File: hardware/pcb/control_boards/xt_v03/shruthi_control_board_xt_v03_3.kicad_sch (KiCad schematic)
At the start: 50 parts, among them IC2 74HC165N, IC3 74HC165N, IC8 74595N, IC9 74HC165N, SW1 Encoder

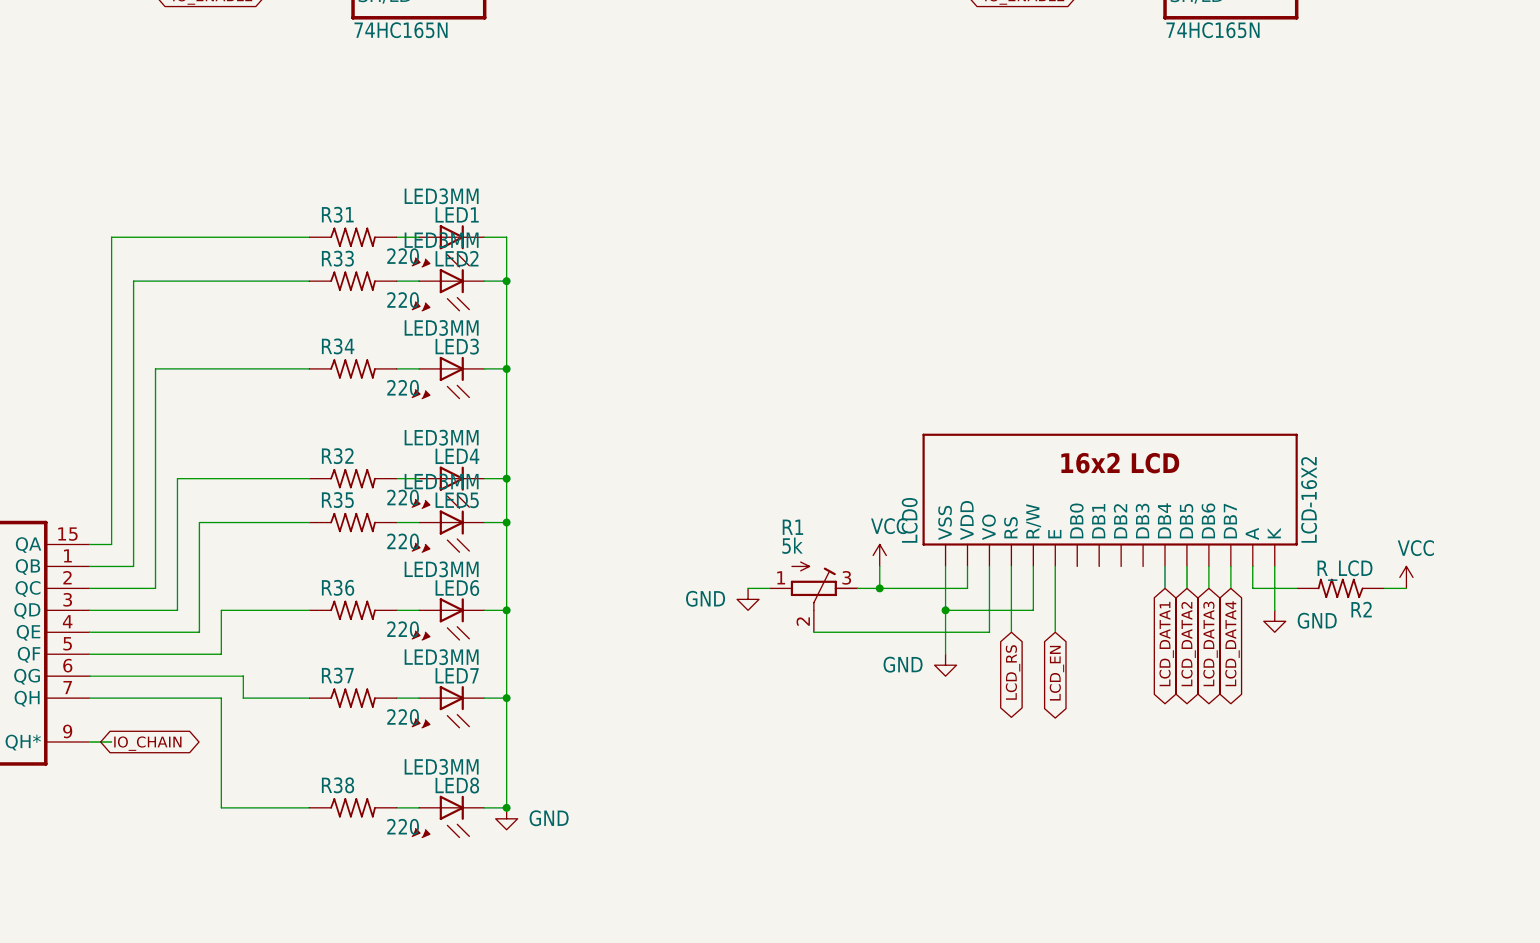
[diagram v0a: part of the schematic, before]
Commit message: update resistors to use kicad symbols
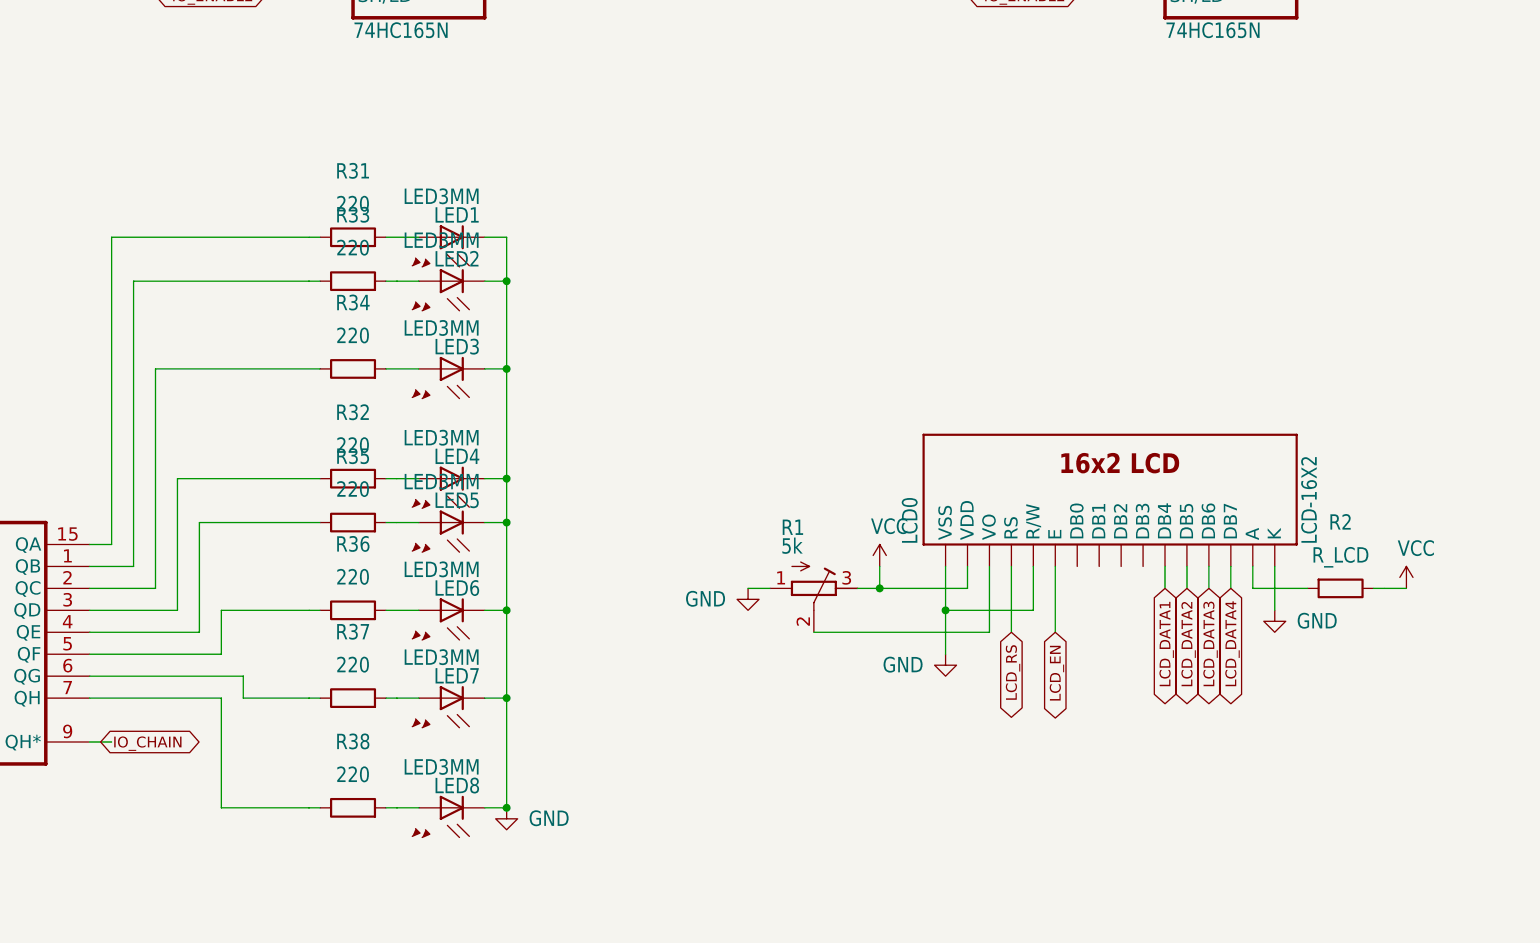
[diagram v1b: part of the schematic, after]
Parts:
- R2, R31, R32, R33, R34, R35, R36, R37, R38: symbol shruthi_control_board_xt_v03-eagle-import:R-US_0204/7 -> Device:R

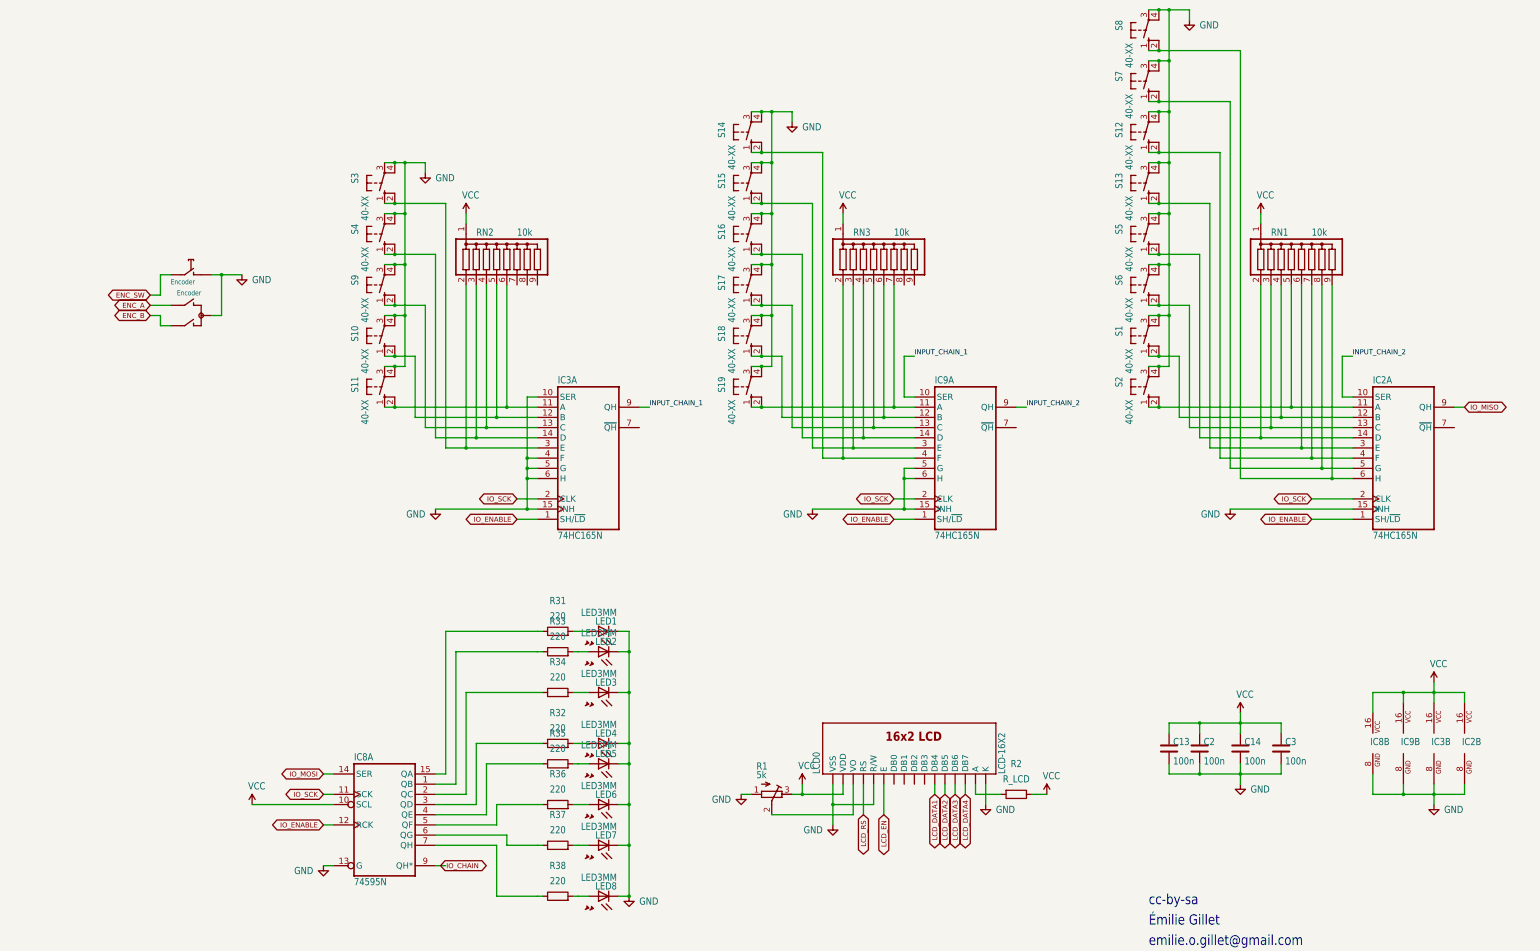
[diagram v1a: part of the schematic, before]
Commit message: update 75HC165s to use kicad symbols
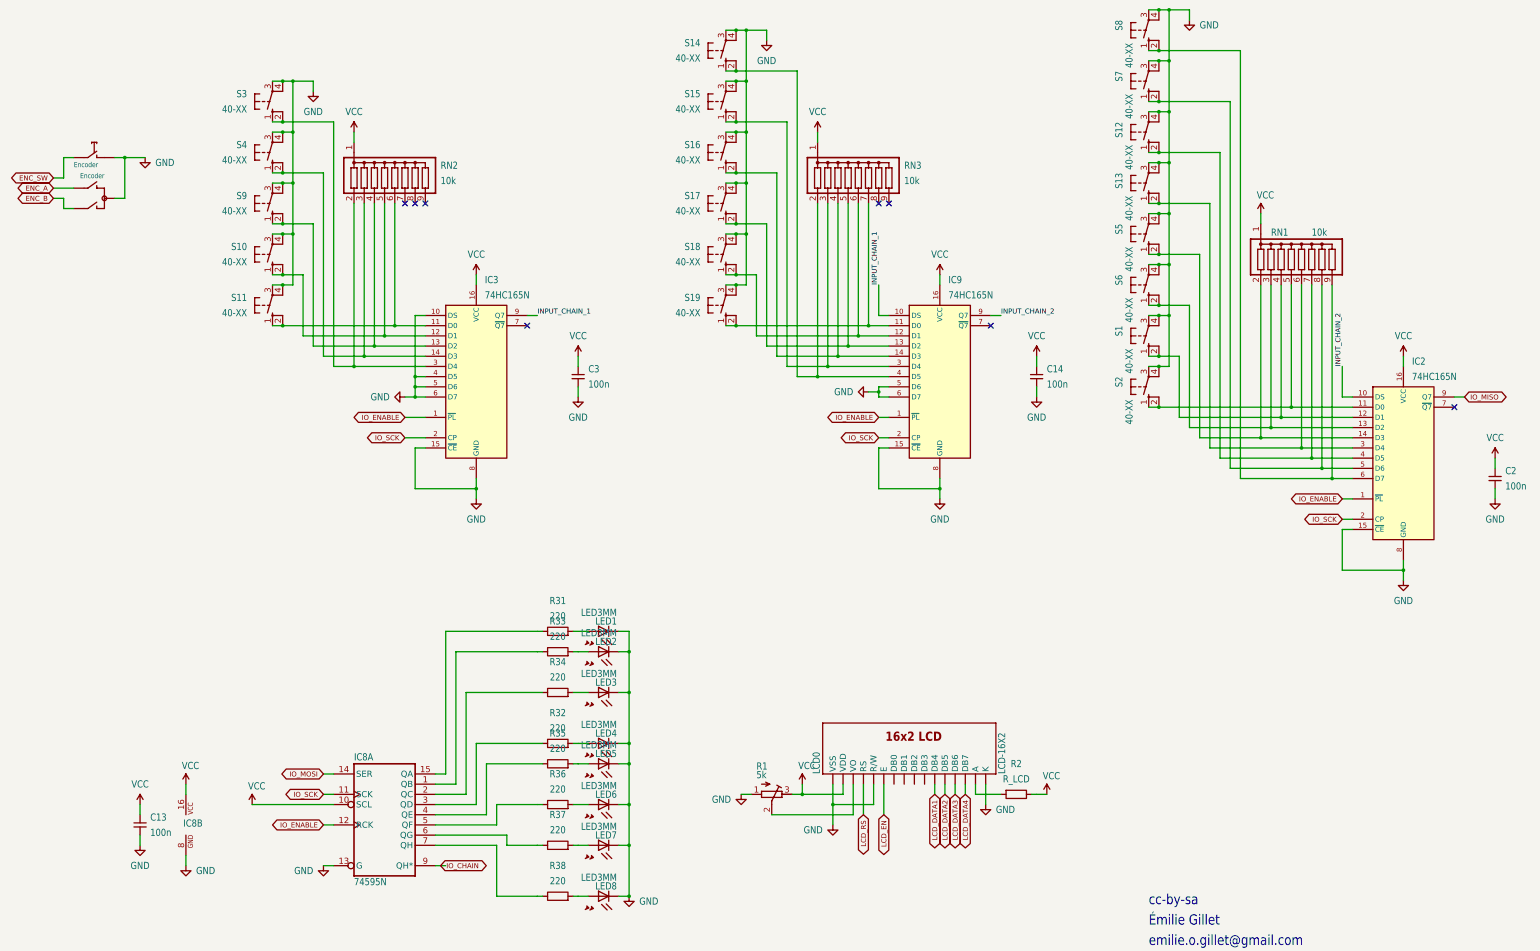
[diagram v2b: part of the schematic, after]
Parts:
- removed unit 2 of IC2
- removed unit 2 of IC3
- removed unit 2 of IC9
- C13, C14, C2, C3: symbol Device:C -> Device:C_Small
- IC2, IC3, IC9: symbol shruthi_control_board_xt_v03-eagle-import:74165N -> 74xx:74HC165
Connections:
- net GND: now also IC2.8 (GND), IC3.8 (GND), IC9.8 (GND)
- net VCC: now also IC2.16 (VCC), IC3.16 (VCC), IC9.16 (VCC)
- no-connect marks 0 -> 8
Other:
- moved on the sheet: C13, C14, C2, C3, RN2, RN3, S10, S11, S14, S15, S16, S17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
